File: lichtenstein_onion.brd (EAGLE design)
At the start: 77.5 x 58.1 mm, 40 parts, among them IC1 LM2852Y-3V3, J1 MAGJACK, U1 ONION-OMEGA2

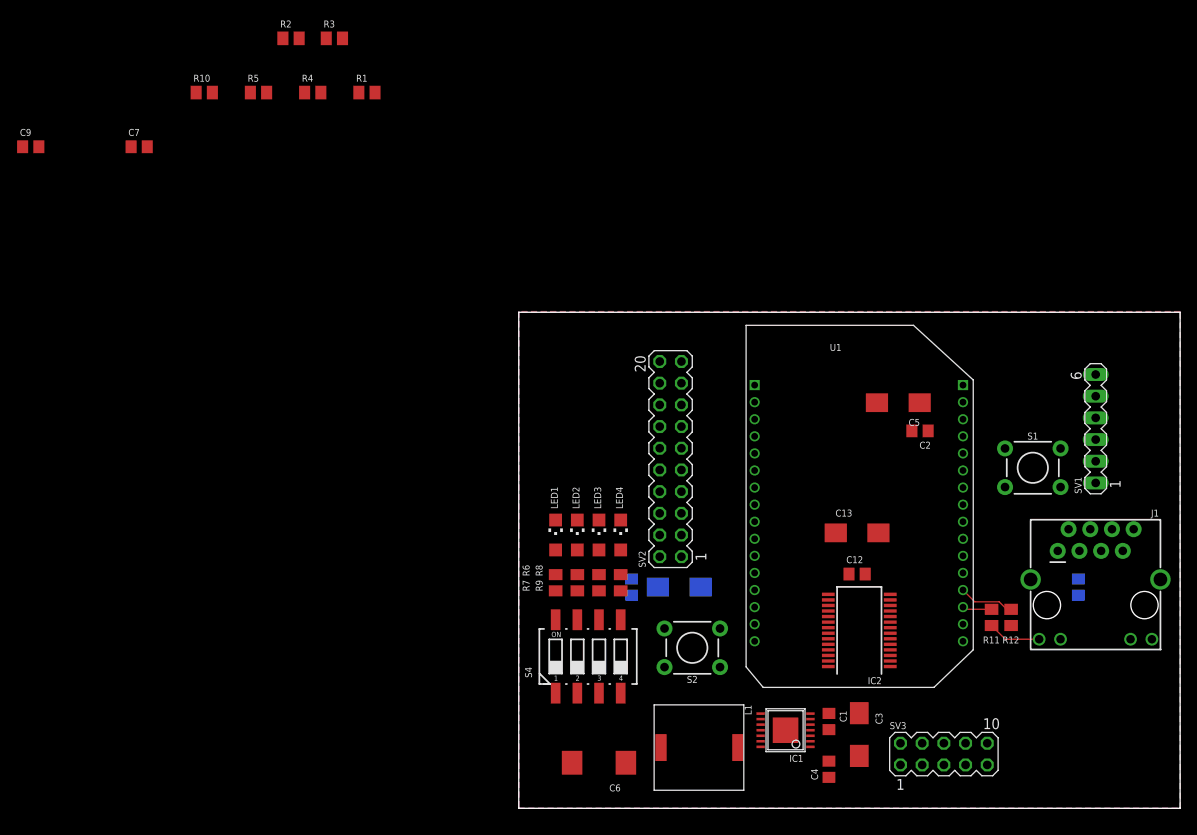
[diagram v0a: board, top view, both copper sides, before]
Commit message: finished main board layout
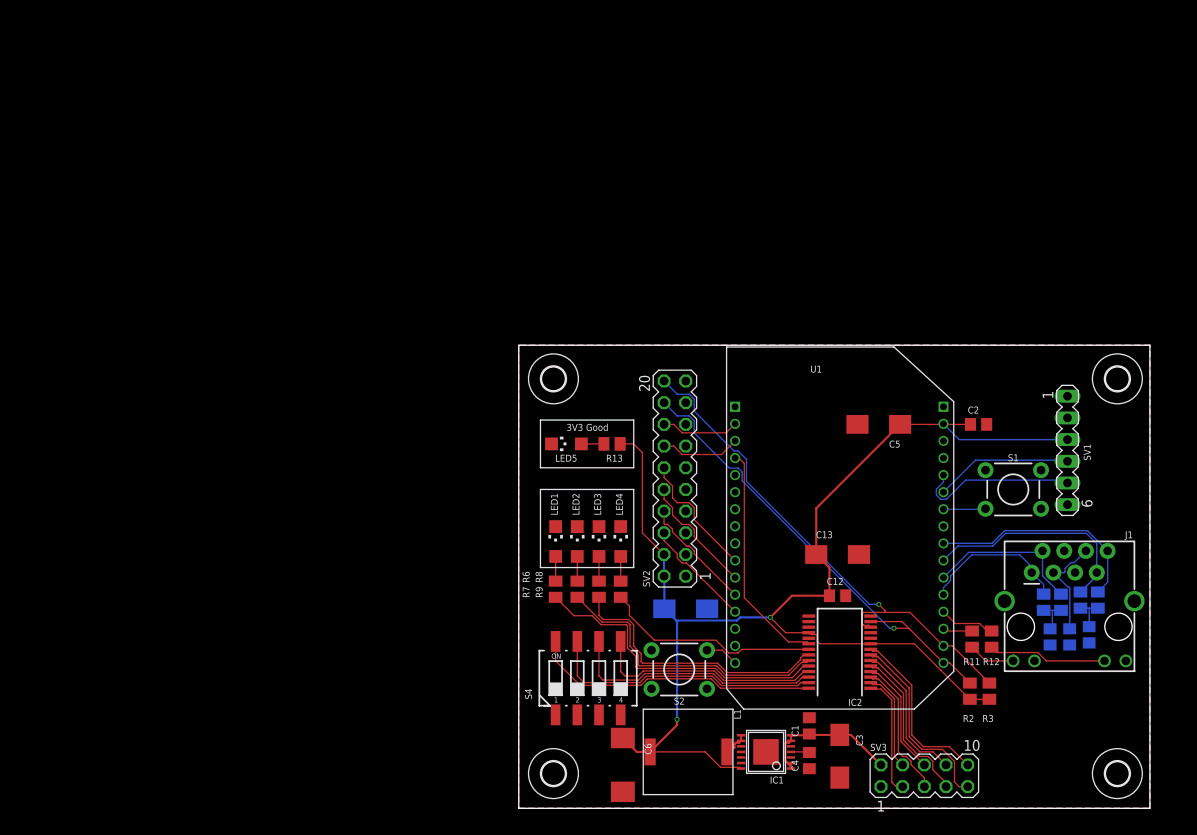
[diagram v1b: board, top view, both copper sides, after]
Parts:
- removed C8: 100nF, rcl:C0805
- added H1, H2, H3, H4: MOUNT-HOLE2.8, holes:2,8
- added LED5: (no value), led:CHIPLED_1206
- added R13: 680R, rcl:M0805
- moved C9 132.5 mm to (62.2, 20.1), flipped to the bottom, turned to 90 degrees
- moved C7 125.1 mm to (66.8, 20.3), flipped to the bottom, turned to 90 degrees
- moved R10 116.7 mm to (63.5, 24.1), flipped to the bottom, turned to 270 degrees
- moved R2 110.3 mm to (52.8, 13.7), turned to 270 degrees
- moved R5 109.6 mm to (61.5, 24.1), flipped to the bottom, turned to 270 degrees
- moved R4 109.5 mm to (67.8, 24.4), flipped to the bottom, turned to 270 degrees
- moved R3 108.3 mm to (55.1, 13.7), turned to 270 degrees
- moved R1 102.5 mm to (65.8, 24.4), flipped to the bottom, turned to 270 degrees
- moved C2 6.90 mm to (53.8, 45.0), turned to 0 degrees
- moved C11 5.93 mm to (64.5, 20.1)
- moved SV1 4.17 mm to (64.3, 41.9), turned to 270 degrees
- moved J1 3.97 mm to (56.9, 10.2)
- moved C13 3.42 mm to (37.3, 29.7)
- moved IC1 3.42 mm to (29.0, 6.60)
- moved SV3 3.42 mm to (47.5, 3.81)
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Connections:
- new net N$1: LED5.A, R13.2
- net +3V3: now also R13.1; no longer C8.1
- net GND: now also LED5.C; no longer C8.2
- net INPUT0: now also IC2.2; no longer IC2.1
- net INPUT1: now also IC2.4; no longer IC2.2
- net INPUT2: now also IC2.6; no longer IC2.3
- net INPUT3: now also IC2.8; no longer IC2.4
- net INPUT4: now also IC2.1; no longer IC2.5
- net INPUT5: now also IC2.3; no longer IC2.6
- net INPUT6: now also IC2.5; no longer IC2.7
- net INPUT7: now also IC2.7; no longer IC2.8
- net STATUS0: now also IC2.24; no longer IC2.25
- net STATUS1: now also IC2.23; no longer IC2.26
- net STATUS2: now also IC2.22; no longer IC2.27
- net STATUS3: now also IC2.21; no longer IC2.28
- net TEST0: now also IC2.25; no longer IC2.21
- net TEST1: now also IC2.26; no longer IC2.22
- net TEST2: now also IC2.27; no longer IC2.23
- net TEST3: now also IC2.28; no longer IC2.24
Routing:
- net +3V3: track 0.00 -> 154.0 mm, vias 0 -> 2
- net I2C_SCL: track 0.00 -> 60.3 mm, vias 0 -> 1
- net I2C_SDA: track 0.00 -> 55.6 mm, vias 0 -> 1
- net STATUS0: track 0.00 -> 36.4 mm
- net TEST3: track 0.00 -> 33.9 mm
- net STATUS1: track 0.00 -> 33.8 mm
- net STATUS2: track 0.00 -> 32.5 mm
- net TEST2: track 0.00 -> 32.4 mm
- net TEST1: track 0.00 -> 29.9 mm
- net TEST0: track 0.00 -> 26.9 mm
- net I2C_INT: track 0.00 -> 26.9 mm
- net ETH_TX+: track 0.00 -> 26.2 mm
- net ETH_TX-: track 0.00 -> 26.1 mm
- net STATUS3: track 0.00 -> 25.5 mm
- net INPUT7: track 0.00 -> 22.5 mm
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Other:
- board size 77.5 x 58.1 mm -> 73.9 x 54.2 mm
- board text added: "3V3 Good"

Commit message: Rev01 sent to manufacture
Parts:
- moved C6 1.02 mm to (11.2, 5.08)
- moved L1 0.51 mm to (23.9, 6.60)
- moved S4 0.51 mm to (8.13, 15.7)
- moved C7 0.25 mm to (66.8, 20.1)
- moved R10 0.25 mm to (63.5, 24.4)
- moved R5 0.25 mm to (61.5, 24.4)
- moved R11 0.25 mm to (52.8, 19.8)
- moved R12 0.25 mm to (55.1, 19.8)
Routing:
- net +3V3: track 154.0 -> 155.1 mm
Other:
- board text added: "Lichtenstein-Onion Rev 01 (c) Tristan Seifert 2018"

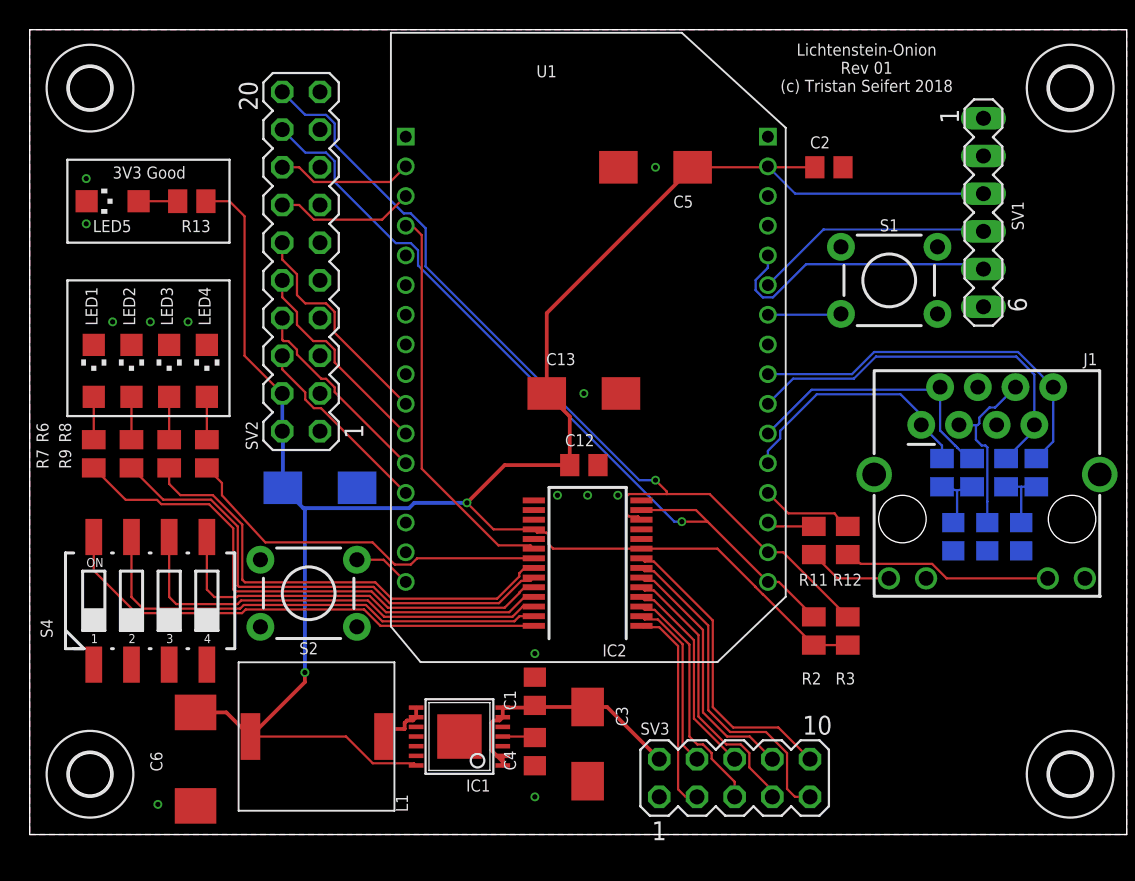
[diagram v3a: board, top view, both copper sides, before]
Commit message: Fixed a few footprint issues and added explcit pull-ups for test inputs
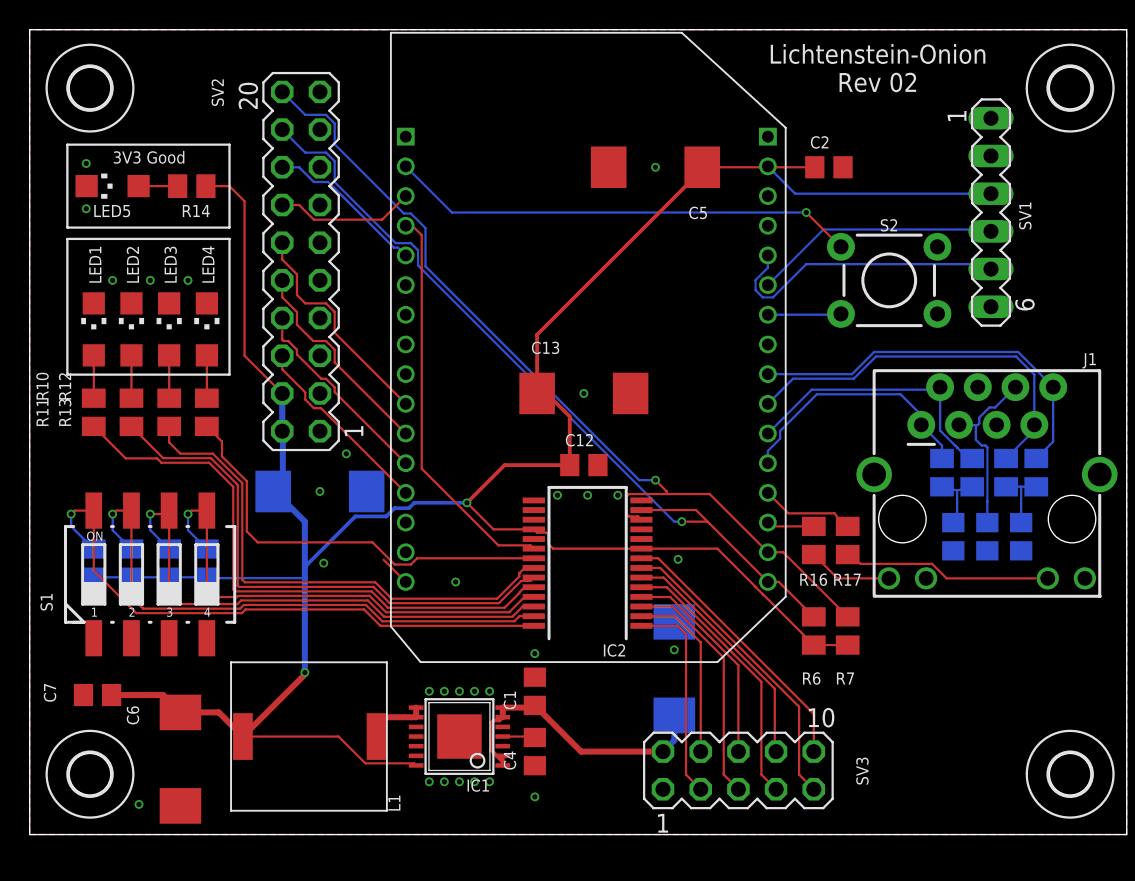
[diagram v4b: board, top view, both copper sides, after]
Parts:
- removed S4: 219-04, switch-dil:CTS-219-04
- added C8: 100nF, rcl:C0805
- added R14, R16, R17: 680R, rcl:M0805
- added R15: 49.9R, rcl:M0805
- C10: value 47µF -> 100nF; device rcl:CT6032 -> rcl:C0805
- C13, C3, C5: value 47µF -> 100µF; device rcl:CT6032 -> rcl:SMC_D
- C9: value 100nF -> 100µF; device rcl:C0805 -> rcl:SMC_D
- R1, R4: value 49.9R -> 10k
- R10: value 49.9R -> 680R
- R2, R3: value 4k7 -> 10k
- R6, R7: value 680R -> 4k7
- R8, R9: value 680R -> 49.9R
- S1: value (none) -> 219-04; device SparkFun-Switches:TACTILE_SWITCH_PTH_6.0MM -> switch-dil:CTS-219-04
- moved H1 66.0 mm to (4.06, 4.06)
- moved H2 66.0 mm to (70.1, 4.06)
- moved R4 63.8 mm to (4.32, 18.3)
- moved C7 63.1 mm to (4.57, 9.40), flipped to the top, turned to 180 degrees
- moved R10 59.3 mm to (4.32, 28.4), flipped to the top, turned to 90 degrees
- moved R8 58.4 mm to (67.8, 24.4), flipped to the bottom, turned to 270 degrees
- moved R1 54.2 mm to (11.9, 18.3)
- moved S1 53.6 mm to (8.13, 17.5)
- moved R6 50.0 mm to (52.8, 13.7), turned to 270 degrees
- moved R7 49.7 mm to (55.1, 13.7), turned to 270 degrees
- moved R9 49.5 mm to (61.5, 24.4), flipped to the bottom, turned to 270 degrees
- moved R3 48.5 mm to (6.86, 18.3), flipped to the bottom
- moved R11 46.8 mm to (6.86, 28.4)
- moved R12 46.5 mm to (9.40, 28.4)
- moved S2 44.4 mm to (57.9, 37.3), turned to 0 degrees
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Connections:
- new net VDD25: S2.1, U1.J2-2
- net !FACTORY_RST: now also S2.3; no longer S1.3
- net !OMEGA_RST: no longer S2.3
- net !OUT_RESET: now also U1.J2-5; no longer U1.J2-2
- net +3V3: now also C7.1, C9.+, R1.2, R14.1, R4.2, R6.2, R7.2; no longer C10.+, R13.1
- net ETH_LED_ACT: now also R16.2; no longer R11.2
- net ETH_LED_LINK: now also R17.2; no longer R12.2
- net ETH_RX+: now also R9.1; no longer R5.1
- net ETH_RX-: now also R15.1; no longer R10.1
- net ETH_TX+: now also R5.1; no longer R1.1
- net ETH_TX-: now also R8.1; no longer R4.1
- net GND: now also C10.1, C7.2, C8.1, C9.-, S1.2, S1.3, S1.4; no longer C10.-, C7.1, C9.1, S2.1, S4.1, S4.2, S4.3, S4.4
- net I2C_SCL: now also R7.1; no longer R3.1
- net I2C_SDA: now also R6.1; no longer R2.1
- net N$1: now also R14.2; no longer R13.2
- net N$10: now also R12.2; no longer R8.2
- net N$11: now also R13.2; no longer R9.2
- net N$2: now also R10.2; no longer R6.2
- net N$3: now also C8.2, R5.2, R8.2; no longer C7.2, R1.2, R4.2
- net N$4: now also R16.1; no longer R11.1
- net N$5: now also R17.1; no longer R12.1
- net N$6: now also C10.2, R15.2, R9.2; no longer C9.2, R10.2, R5.2
- net N$9: now also R11.2; no longer R7.2
- net STATUS0: now also R10.1; no longer R6.1
- net STATUS1: now also R11.1; no longer R7.1
- net STATUS2: now also R12.1; no longer R8.1
- net STATUS3: now also R13.1; no longer R9.1
- net TEST0: now also R1.1, S1.5; no longer S4.5
- net TEST1: now also R2.1, S1.6; no longer S4.6
- net TEST2: now also R3.1, S1.7; no longer S4.7
- net TEST3: now also R4.1, S1.8; no longer S4.8
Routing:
- net VDD25: track 0.00 -> 31.6 mm, vias 0 -> 1
- net +3V3: track 155.1 -> 180.0 mm
- net TEST3: track 33.7 -> 40.0 mm, vias 0 -> 1
- net TEST0: track 26.7 -> 32.7 mm, vias 0 -> 1
- net TEST2: track 32.2 -> 38.2 mm, vias 0 -> 1
- net TEST1: track 29.7 -> 35.6 mm, vias 0 -> 1
- net STATUS3: track 25.5 -> 28.6 mm
- net V+: track 17.6 -> 20.5 mm
- net STATUS1: track 33.9 -> 36.7 mm
- net STATUS0: track 36.6 -> 39.4 mm
- net STATUS2: track 32.0 -> 34.8 mm
- net INPUT7: track 22.5 -> 20.5 mm
- net INPUT3: track 20.4 -> 18.5 mm
- net !OMEGA_RST: track 3.91 -> 2.12 mm
- net !OUT_RESET: track 9.17 -> 10.8 mm
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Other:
- board text added: "(c) Tristan Seifert 2018"
- board text added: "Lichtenstein-Onion Rev 02"
- board text removed: "Lichtenstein-Onion Rev 01 (c) Tristan Seifert 2018"

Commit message: Fixed some more footprints on MAX10 driver
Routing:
- net !OMEGA_RST: track 2.12 -> 0.00 mm
- net N$6: track 4.32 -> 5.12 mm
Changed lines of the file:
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@@
 <?xml version="1.0" encoding="utf-8"?>
 <!DOCTYPE eagle SYSTEM "eagle.dtd">
-<eagle version="8.7.0">
+<eagle version="9.0.1">
 <drawing>
 <settings>
@@
 <contactref element="C10" pad="2"/>
 <contactref element="R15" pad="2"/>
-<wire x1="63.5" y1="23.434" x2="62.484" y2="23.18" width="0.1524" layer="16"/>
-<wire x1="62.484" y1="23.18" x2="61.468" y2="23.434" width="0.1524" layer="16"/>
 <wire x1="62.23" y1="21.016" x2="62.484" y2="21.524" width="0.1524" layer="16"/>
-<wire x1="62.484" y1="21.524" x2="62.484" y2="23.18" width="0.1524" layer="16"/>
+<wire x1="61.468" y1="23.434" x2="62.484" y2="23.434" width="0.1524" layer="16"/>
+<wire x1="62.484" y1="23.434" x2="63.5" y2="23.434" width="0.1524" layer="16"/>
+<wire x1="62.23" y1="21.016" x2="62.484" y2="21.27" width="0.1524" layer="16"/>
+<wire x1="62.484" y1="21.27" x2="62.484" y2="23.434" width="0.1524" layer="16"/>
 </signal>
 <signal name="N$3">
@@
 <signal name="!OMEGA_RST">
 <contactref element="U1" pad="J2-16"/>
-<wire x1="25.338" y1="17.02" x2="23.8414" y2="18.5166" width="0.1524" layer="1"/>
 </signal>
 <signal name="TEST3">
